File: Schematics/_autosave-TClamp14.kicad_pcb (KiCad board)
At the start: 2 copper layers, 60 x 13 mm, 6 parts, among them J1 FTSH-107-01-L-DV-K-A, J2 Conn_02x07_Odd_Even

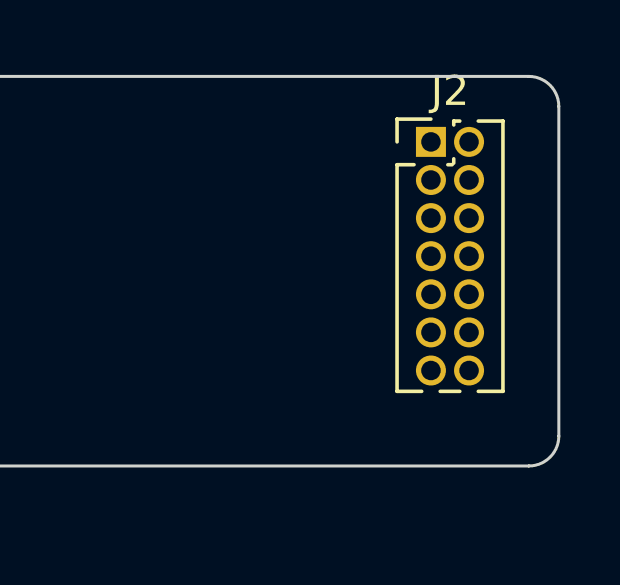
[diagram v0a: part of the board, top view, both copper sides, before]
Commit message: Decide on standard and started routing
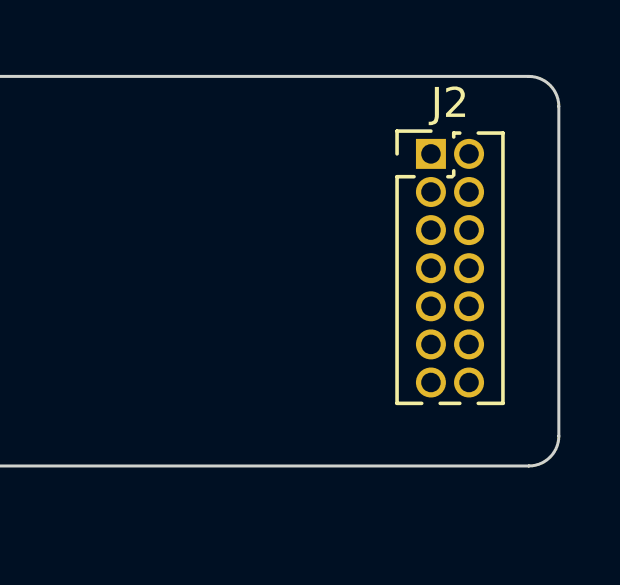
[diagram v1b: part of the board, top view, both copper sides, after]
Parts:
- moved J2 0.40 mm to (171.2, 52.1)
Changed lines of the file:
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@@
   )
   (footprint "Connector_PinHeader_1.27mm:PinHeader_2x07_P1.27mm_Vertical" (layer "F.Cu")
-    (at 171.23 51.69)
+    (at 171.23 52.09)
     (descr "Through hole straight pin header, 2x07, 1.27mm pitch, double rows")
     (tags "Through hole pin header THT 2x07 1.27mm double row")
